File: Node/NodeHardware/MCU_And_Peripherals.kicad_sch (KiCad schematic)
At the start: 87 parts, among them Q4 2N7002, Q5 2N7002, SW1 RST, SW2 BOOT, SW3 BTN, U7 ESP32-S3-WROOM-1, U8 UCC27511ADBV

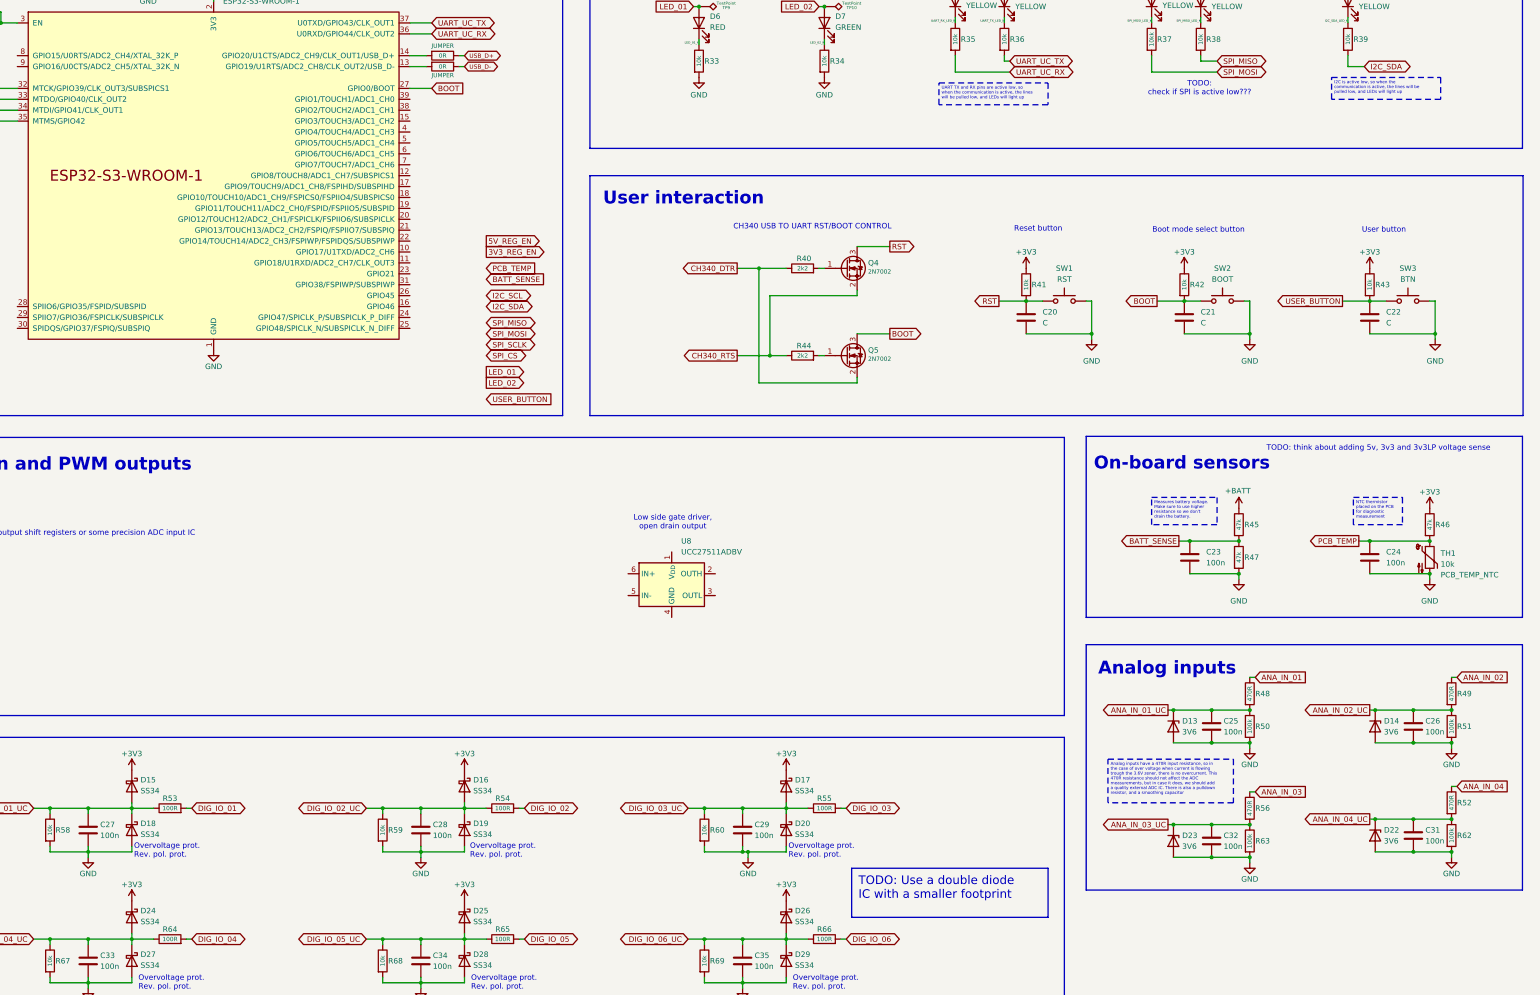
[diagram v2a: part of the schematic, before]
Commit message: Update SCHM (psu, cleanup), add datasheets
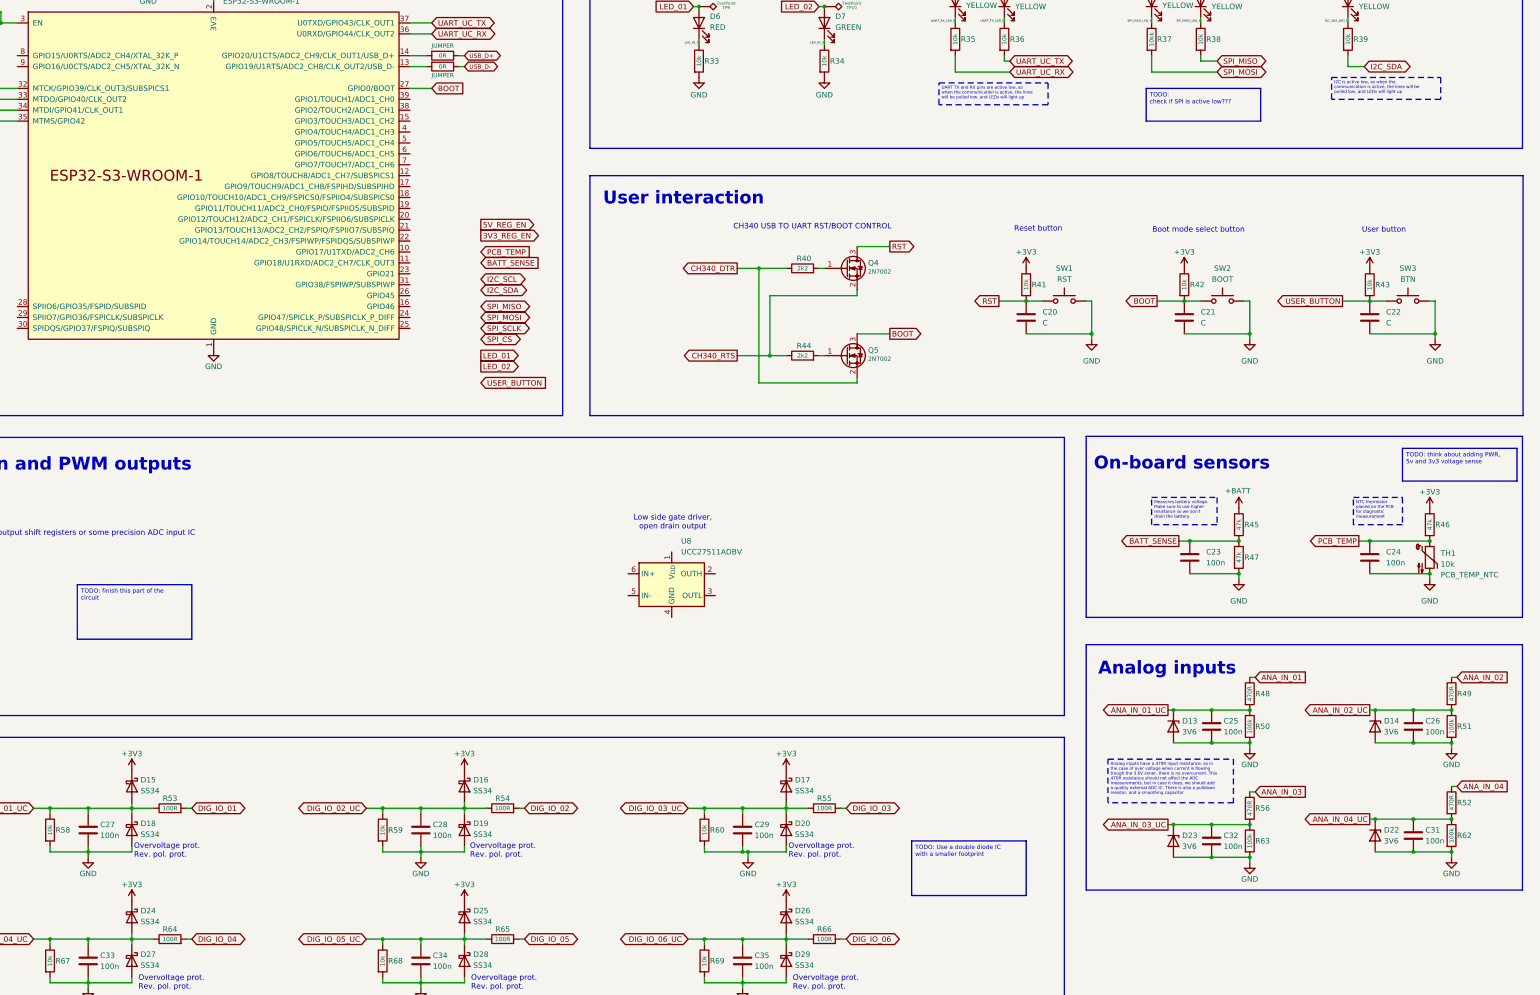
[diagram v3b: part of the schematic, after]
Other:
- note removed: "TODO: check if SPI is active low???"
- note removed: "TODO: think about adding 5v, 3v3 and 3v3LP voltage sense"
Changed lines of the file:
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@@
 		)
 	)
-	(text_box "TODO: Use a double diode IC with a smaller footprint"
-		(exclude_from_sim no)
-		(at 245.11 243.84 0)
-		(size 45.72 11.43)
+	(text_box "TODO:\ncheck if SPI is active low???"
+		(exclude_from_sim no)
+		(at 313.69 62.23 0)
+		(size 26.67 7.62)
 		(stroke
 			(width 0)
@@
 		)
 		(fill
-			(type none)
-		)
-		(effects
-			(font
-				(size 2 2)
+			(type color)
+			(color 250 250 100 1)
+		)
+		(effects
+			(font
+				(size 1 1)
 			)
 			(justify left top)
@@
 		)
 	)
+	(text_box "TODO: Use a double diode IC with a smaller footprint"
+		(exclude_from_sim no)
+		(at 259.08 237.49 0)
+		(size 26.67 12.7)
+		(stroke
+			(width 0)
+			(type default)
+		)
+		(fill
+			(type color)
+			(color 250 250 100 1)
+		)
+		(effects
+			(font
+				(size 1 1)
+			)
+			(justify left top)
+		)
+	)
 	(text_box "SPI activity LEDs"
 		(exclude_from_sim no)
@@
 		)
 	)
+	(text_box "TODO: think about adding PWR, 5v and 3v3 voltage sense"
+		(exclude_from_sim no)
+		(at 373.38 146.05 0)
+		(size 26.67 7.62)
+		(stroke
+			(width 0)
+			(type default)
+		)
+		(fill
+			(type color)
+			(color 250 250 100 1)
+		)
+		(effects
+			(font
+				(size 1 1)
+			)
+			(justify left top)
+		)
+	)
 	(text_box "Analog inputs have a 470R input resistance, so in the case of over voltage when current is flowing trough the 3.6V zener, there is no overcurrent. This 470R resistance should not affect the ADC measurements, but in case it does, we should add a quality external ADC IC. There is also a pulldown resistor, and a smoothing capacitor"
 		(exclude_from_sim no)
@@
 		)
 	)
-	(text "TODO: think about adding 5v, 3v3 and 3v3LP voltage sense"
-		(exclude_from_sim no)
-		(at 367.792 146.05 0)
-		(effects
-			(font
-				(size 1.27 1.27)
-			)
+	(text_box "TODO: finish this part of the circuit"
+		(exclude_from_sim no)
+		(at 64.77 177.8 0)
+		(size 26.67 12.7)
+		(stroke
+			(width 0)
+			(type default)
+		)
+		(fill
+			(type color)
+			(color 250 250 100 1)
+		)
+		(effects
+			(font
+				(size 1 1)
+			)
+			(justify left top)
 		)
 	)
@@
 		)
 	)
-	(text "TODO:\ncheck if SPI is active low???"
-		(exclude_from_sim no)
-		(at 326.136 62.23 0)
-		(effects
-			(font
-				(size 1.27 1.27)
-			)
-		)
-	)
 	(text "MCU"
 		(exclude_from_sim no)
@@
 	(global_label "BATT_SENSE"
 		(shape input)
-		(at 160.02 106.68 0)
-		(fields_autoplaced yes)
-		(effects
-			(font
-				(size 1.27 1.27)
-			)
-			(justify left)
-		)
-		(property "Intersheetrefs" "${INTERSHEET_REFS}"
-			(at 174.3141 106.68 0)
+		(at 158.75 102.87 0)
+		(fields_autoplaced yes)
+		(effects
+			(font
+				(size 1.27 1.27)
+			)
+			(justify left)
+		)
+		(property "Intersheetrefs" "${INTERSHEET_REFS}"
+			(at 173.0441 102.87 0)
 			(effects
 				(font
@@
 	(global_label "SPI_SCLK"
 		(shape bidirectional)
-		(at 160.02 121.92 0)
-		(fields_autoplaced yes)
-		(effects
-			(font
-				(size 1.27 1.27)
-			)
-			(justify left)
-		)
-		(property "Intersheetrefs" "${INTERSHEET_REFS}"
-			(at 172.946 121.92 0)
+		(at 158.75 118.11 0)
+		(fields_autoplaced yes)
+		(effects
+			(font
+				(size 1.27 1.27)
+			)
+			(justify left)
+		)
+		(property "Intersheetrefs" "${INTERSHEET_REFS}"
+			(at 171.676 118.11 0)
 			(effects
 				(font
@@
 	(global_label "LED_02"
 		(shape output)
-		(at 160.02 130.81 0)
-		(fields_autoplaced yes)
-		(effects
-			(font
-				(size 1.27 1.27)
-			)
-			(justify left)
-		)
-		(property "Intersheetrefs" "${INTERSHEET_REFS}"
-			(at 169.8389 130.81 0)
+		(at 158.75 127 0)
+		(fields_autoplaced yes)
+		(effects
+			(font
+				(size 1.27 1.27)
+			)
+			(justify left)
+		)
+		(property "Intersheetrefs" "${INTERSHEET_REFS}"
+			(at 168.5689 127 0)
 			(effects
 				(font
@@
 	(global_label "5V_REG_EN"
 		(shape output)
-		(at 160.02 97.79 0)
-		(fields_autoplaced yes)
-		(effects
-			(font
-				(size 1.27 1.27)
-			)
-			(justify left)
-		)
-		(property "Intersheetrefs" "${INTERSHEET_REFS}"
-			(at 173.407 97.79 0)
+		(at 158.75 93.98 0)
+		(fields_autoplaced yes)
+		(effects
+			(font
+				(size 1.27 1.27)
+			)
+			(justify left)
+		)
+		(property "Intersheetrefs" "${INTERSHEET_REFS}"
+			(at 172.137 93.98 0)
 			(effects
 				(font
@@
 	(global_label "I2C_SDA"
 		(shape bidirectional)
-		(at 160.02 113.03 0)
-		(fields_autoplaced yes)
-		(effects
-			(font
-				(size 1.27 1.27)
-			)
-			(justify left)
-		)
-		(property "Intersheetrefs" "${INTERSHEET_REFS}"
-			(at 171.7365 113.03 0)
+		(at 158.75 109.22 0)
+		(fields_autoplaced yes)
+		(effects
+			(font
+				(size 1.27 1.27)
+			)
+			(justify left)
+		)
+		(property "Intersheetrefs" "${INTERSHEET_REFS}"
+			(at 170.4665 109.22 0)
 			(effects
 				(font
@@
 	(global_label "SPI_CS"
 		(shape bidirectional)
-		(at 160.02 124.46 0)
-		(fields_autoplaced yes)
-		(effects
-			(font
-				(size 1.27 1.27)
-			)
-			(justify left)
-		)
-		(property "Intersheetrefs" "${INTERSHEET_REFS}"
-			(at 170.6479 124.46 0)
+		(at 158.75 120.65 0)
+		(fields_autoplaced yes)
+		(effects
+			(font
+				(size 1.27 1.27)
+			)
+			(justify left)
+		)
+		(property "Intersheetrefs" "${INTERSHEET_REFS}"
+			(at 169.3779 120.65 0)
 			(effects
 				(font
@@
 	(global_label "I2C_SCL"
 		(shape bidirectional)
-		(at 160.02 110.49 0)
-		(fields_autoplaced yes)
-		(effects
-			(font
-				(size 1.27 1.27)
-			)
-			(justify left)
-		)
-		(property "Intersheetrefs" "${INTERSHEET_REFS}"
-			(at 171.676 110.49 0)
+		(at 158.75 106.68 0)
+		(fields_autoplaced yes)
+		(effects
+			(font
+				(size 1.27 1.27)
+			)
+			(justify left)
+		)
+		(property "Intersheetrefs" "${INTERSHEET_REFS}"
+			(at 170.406 106.68 0)
 			(effects
 				(font
@@
 	(global_label "PCB_TEMP"
 		(shape input)
-		(at 160.02 104.14 0)
-		(fields_autoplaced yes)
-		(effects
-			(font
-				(size 1.27 1.27)
-			)
-			(justify left)
-		)
-		(property "Intersheetrefs" "${INTERSHEET_REFS}"
-			(at 172.6208 104.14 0)
+		(at 158.75 100.33 0)
+		(fields_autoplaced yes)
+		(effects
+			(font
+				(size 1.27 1.27)
+			)
+			(justify left)
+		)
+		(property "Intersheetrefs" "${INTERSHEET_REFS}"
+			(at 171.3508 100.33 0)
 			(effects
 				(font
@@
 	(global_label "3V3_REG_EN"
 		(shape output)
-		(at 160.02 100.33 0)
-		(fields_autoplaced yes)
-		(effects
-			(font
-				(size 1.27 1.27)
-			)
-			(justify left)
-		)
-		(property "Intersheetrefs" "${INTERSHEET_REFS}"
-			(at 174.6165 100.33 0)
+		(at 158.75 96.52 0)
+		(fields_autoplaced yes)
+		(effects
+			(font
+				(size 1.27 1.27)
+			)
+			(justify left)
+		)
+		(property "Intersheetrefs" "${INTERSHEET_REFS}"
+			(at 173.3465 96.52 0)
 			(effects
 				(font
@@
 	(global_label "LED_01"
 		(shape output)
-		(at 160.02 128.27 0)
-		(fields_autoplaced yes)
-		(effects
-			(font
-				(size 1.27 1.27)
-			)
-			(justify left)
-		)
-		(property "Intersheetrefs" "${INTERSHEET_REFS}"
-			(at 169.8389 128.27 0)
+		(at 158.75 124.46 0)
+		(fields_autoplaced yes)
+		(effects
+			(font
+				(size 1.27 1.27)
+			)
+			(justify left)
+		)
+		(property "Intersheetrefs" "${INTERSHEET_REFS}"
+			(at 168.5689 124.46 0)
 			(effects
 				(font
@@
 	(global_label "SPI_MISO"
 		(shape bidirectional)
-		(at 160.02 116.84 0)
-		(fields_autoplaced yes)
-		(effects
-			(font
-				(size 1.27 1.27)
-			)
-			(justify left)
-		)
-		(property "Intersheetrefs" "${INTERSHEET_REFS}"
-			(at 172.7646 116.84 0)
+		(at 158.75 113.03 0)
+		(fields_autoplaced yes)
+		(effects
+			(font
+				(size 1.27 1.27)
+			)
+			(justify left)
+		)
+		(property "Intersheetrefs" "${INTERSHEET_REFS}"
+			(at 171.4946 113.03 0)
 			(effects
 				(font
@@
 	(global_label "USER_BUTTON"
 		(shape input)
-		(at 160.02 134.62 0)
-		(fields_autoplaced yes)
-		(effects
-			(font
-				(size 1.27 1.27)
-			)
-			(justify left)
-		)
-		(property "Intersheetrefs" "${INTERSHEET_REFS}"
-			(at 176.1285 134.62 0)
+		(at 158.75 130.81 0)
+		(fields_autoplaced yes)
+		(effects
+			(font
+				(size 1.27 1.27)
+			)
+			(justify left)
+		)
+		(property "Intersheetrefs" "${INTERSHEET_REFS}"
+			(at 174.8585 130.81 0)
 			(effects
 				(font
@@
 	(global_label "SPI_MOSI"
 		(shape bidirectional)
-		(at 160.02 119.38 0)
-		(fields_autoplaced yes)
-		(effects
-			(font
-				(size 1.27 1.27)
-			)
-			(justify left)
-		)
-		(property "Intersheetrefs" "${INTERSHEET_REFS}"
-			(at 172.7646 119.38 0)
-			(effects
-				(font
+		(at 158.75 115.57 0)
+		(fields_autoplaced yes)
+		(effects
+			(font
+				(size 1.27 1.27)
+			)
+			(justify left)
+		)
+		(property "Intersheetrefs" "${INTERSHEET_REFS}"
+			(at 171.4946 115.57 0)
+			(effects
+				(font

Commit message: Continue updating schm for initial version
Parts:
- removed C23: 100n, Capacitor_SMD:C_0805_2012Metric, symbol Device:C
- added C10, C11, C8, C9: 100n, Capacitor_SMD:C_0805_2012Metric, symbol Device:C
- added D21, D5: YELLOW, LED_SMD:LED_1210_3225Metric, symbol Device:LED
- added R10, R11, R12, R30, R31, R9: 47k, Resistor_SMD:R_0805_2012Metric, symbol Device:R
- added R26, R28: 10k, Resistor_SMD:R_0805_2012Metric, symbol Device:R
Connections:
- net +3V3: now also D21.2 (A), D5.2 (A), R11.1
- net +BATT: now also R9.1; no longer R45.1
- net ANA_IN_01_UC: now also U7.38 (GPIO2/TOUCH2/ADC1_CH1)
- net ANA_IN_02_UC: now also U7.15 (GPIO3/TOUCH3/ADC1_CH2)
- net ANA_IN_03_UC: now also U7.4 (GPIO4/TOUCH4/ADC1_CH3)
- net ANA_IN_04_UC: now also U7.5 (GPIO5/TOUCH5/ADC1_CH4)
- net BATT_SENSE: now also C8.1, R10.1, R9.2; no longer R45.2, R47.1
- net GND: now also C10.2, C11.2, C8.2, C9.2, R10.2, R12.2, R31.2
- net UART1_UC_TX: now reaches U7.10 (GPIO17/U1TXD/ADC2_CH6)
- net UART1_UC_TX: now also R28.2
- net UART1_UC_RX: now reaches U7.11 (GPIO18/U1RXD/ADC2_CH7/CLK_OUT3)
- net UART1_UC_RX: now also R26.2
- net UART_RX_LED_K renamed UART0_RX_LED_K
- net UART_TX_LED_K renamed UART0_TX_LED_K
- net UART_UC_RX renamed UART0_UC_RX
- net UART_UC_TX renamed UART0_UC_TX
- new net +5V: R30.1
- new net 3V3_SENSE: C9.1, R11.2, R12.1
- new net 5V_SENSE: C10.1, R30.2, R31.1
- new net PWR_SENSE: C11.1, R45.2, R47.1
- new net UART1_RX_LED_K: D5.1 (K), R26.1
- new net UART1_TX_LED_K: D21.1 (K), R28.1
- new net V_IN: R45.1
- no-connect marks 0 -> 8
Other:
- note added: "ADC"
- note added: "ADC1 CH0-CH4"
- note added: "DIRECT USB"
- note added: "ESP32-S3-WROOM-1-N16R8"
- note added: "GSM MODULE"
- note added: "IN/OUT"
- note added: "JTAG DEBUGGING"
- note added: "USB TO UART PROGRAMMING"
- moved on the sheet: C24, D10, D11, D12, D6, D7, D8, D9, R33, R34, R35, R36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

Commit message: Continue schm update, slow progress
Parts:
- removed U8: UCC27511ADBV, Package_TO_SOT_SMD:SOT-23-6, symbol Driver_FET:UCC27511ADBV
- added C19, C23: 100n, Capacitor_SMD:C_0805_2012Metric, symbol Device:C
- added R61, R70: ???, Resistor_SMD:R_0805_2012Metric, symbol Device:R
- added U10, U6: UCC27517DBVR, UCC27517DBVR:UCC27517DBVR_DBV5_TEX, symbol UCC27517DBVR:UCC27517DBVR
- added U11, U8: IRLR024NTRPBF, IRLR024NTRPBF:IRLR024NTRPBF_PG-TO252-3_INF, symbol IRLR024NTRPBF:IRLR024NTRPBF
- added U4: ADS1220xPW, Package_SO:TSSOP-16_4.4x5mm_P0.65mm, symbol Analog_ADC:ADS1220xPW
- U7: footprint Espressif:ESP32-S3-WROOM-1 -> RF_Module:ESP32-S3-WROOM-1
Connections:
- net +3V3: now also C19.2, C23.2, U4.12 (AVDD), U4.13 (DVDD)
- net +5V: now also U10.1 (VDD), U6.1 (VDD)
- net 3V3_SENSE: now also U4.11 (AIN0/REFP1)
- net 5V_SENSE: now also U4.10 (AIN1)
- net BATT_SENSE: now also U4.7 (AIN2)
- net GND: now also C19.1, C23.1, U10.2 (GND), U10.4 (IN-), U11.3 (S), U4.3 (CLK), U4.4 (DGND), U4.5 (AVSS), U6.2 (GND), U6.4 (IN-), U8.3 (S)
- net PCB_TEMP: now also U7.39 (GPIO1/TOUCH1/ADC1_CH0)
- net PWR_SENSE: now also U4.6 (AIN3/REFN1)
- net SPI_MISO: now also U4.15 (DOUT/~{DRDY})
- net SPI_MOSI: now also U4.16 (DIN)
- net SPI_SCLK: now also U4.1 (SCLK)
- new net: R70.1, U10.5 (OUT)
- new net: R70.2, U11.1 (G)
- new net: R61.2, U8.1 (G)
- new net: R61.1, U6.5 (OUT)
- new net DIG_OUT_01: U8.2 (D)
- new net DIG_OUT_01_UC: U6.3 (IN+)
- new net DIG_OUT_02: U11.2 (D)
- new net DIG_OUT_02_UC: U10.3 (IN+)
- new net SPI_CS_ADC: U4.2 (~{CS})
- no-connect marks 8 -> 10
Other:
- note added: "ADC via SPI ADS1220IPWR"
- note added: "DIG IN/OUT"
- note added: "IRLR024NTRPBF N MOSFET"
- note added: "UCC27517DBVR Low side gate driver, open drain output"
- note removed: "ADC"
- note removed: "IN/OUT"
- note removed: "If needed, use output shift registers or some precision ADC input IC"
- note removed: "Low side gate driver, open drain output"
